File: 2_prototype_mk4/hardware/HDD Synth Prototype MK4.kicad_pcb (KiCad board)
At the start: 2 copper layers, 100.3 x 69.9 mm, 44 parts, among them J1 Micro_SD_Card, J3 Conn_02x20_Odd_Even, J4 1734451-1, J5 Conn_01x03_Pin, J6 171825-4, J7 Conn_01x04_Pin, J8 Conn_01x05, U1 MAX98357A, U2 Optocoupler_DC_PhotoNPN_AKEC, U3 TXS0101DBV

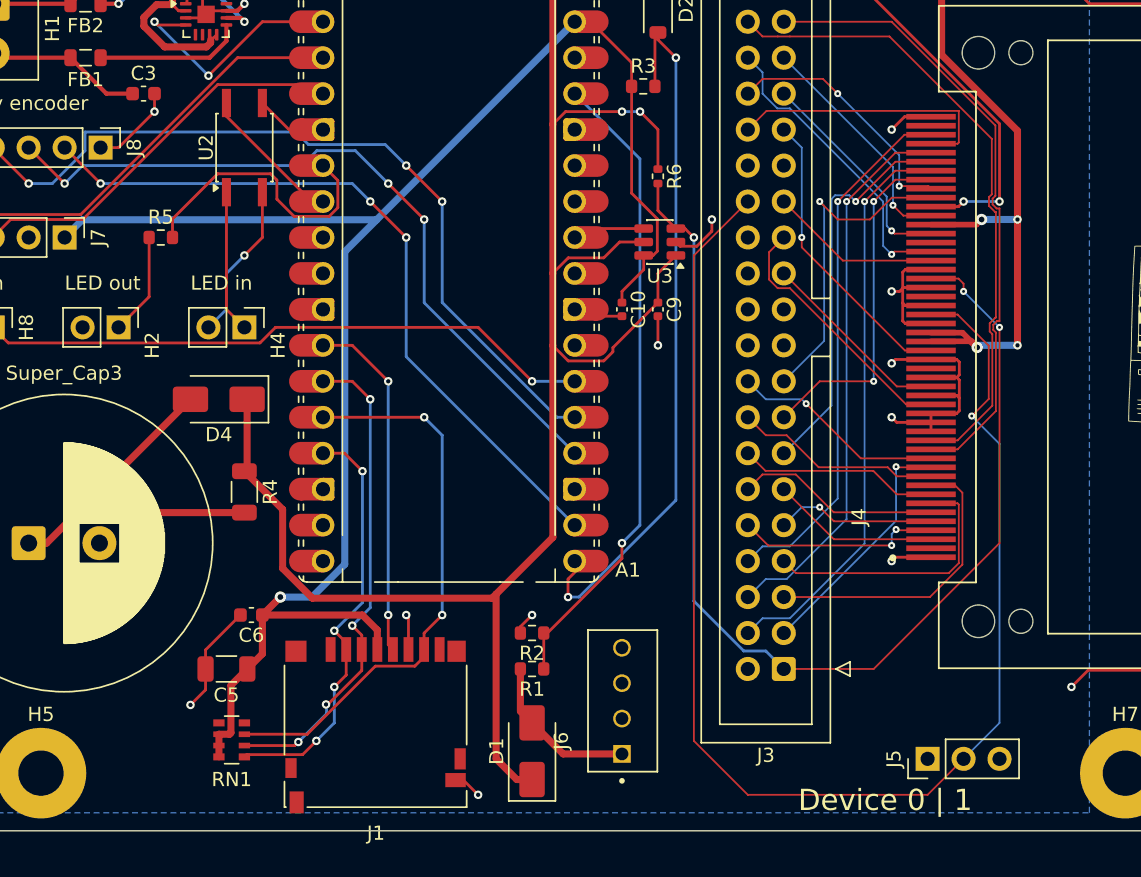
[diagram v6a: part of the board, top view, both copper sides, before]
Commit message: MKIV add RGB LED, reset jumper and fixed reset circuit
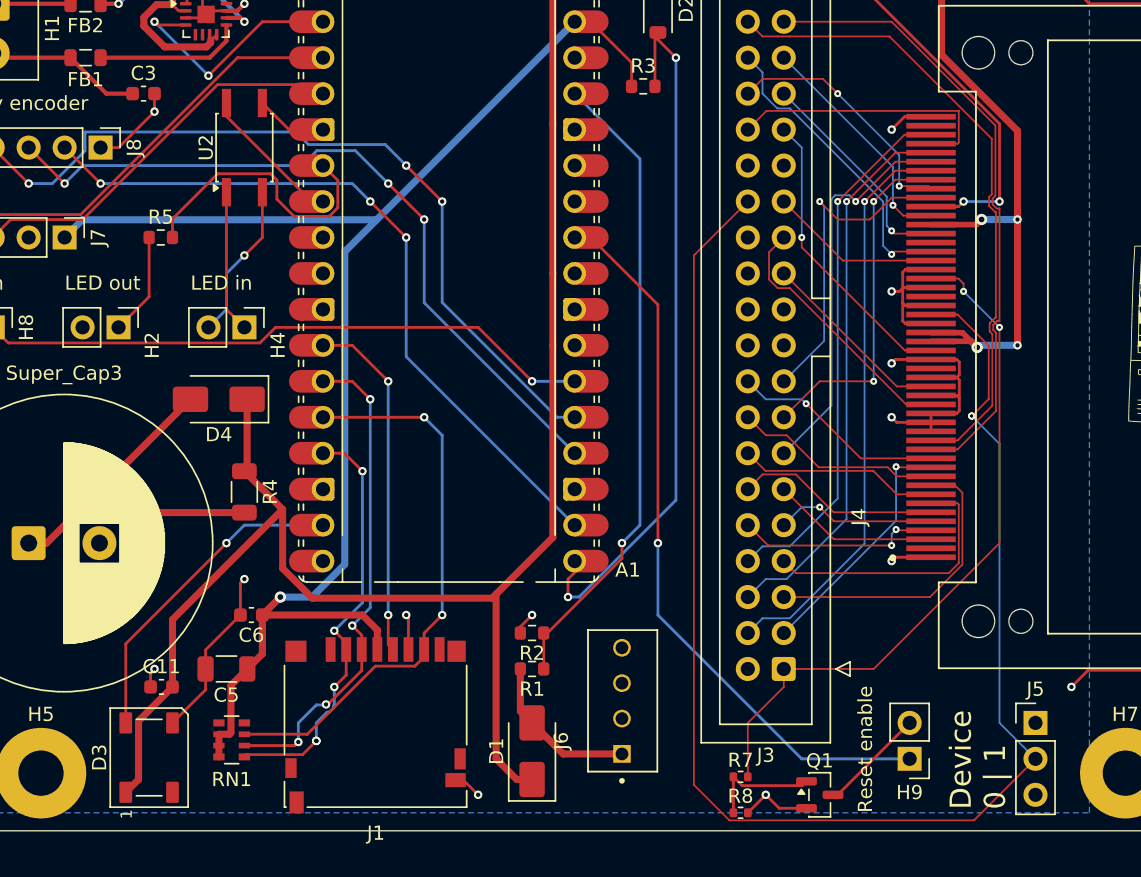
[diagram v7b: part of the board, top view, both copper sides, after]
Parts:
- removed C10, C9: 100nF, Capacitor_SMD:C_0402_1005Metric
- removed R6: 10K, Resistor_SMD:R_0402_1005Metric
- removed U3: TXS0101DBV, Package_TO_SOT_SMD:SOT-23-6
- added C11: 0.1uF, Capacitor_SMD:C_0603_1608Metric, F.Cu at (91.9, 106.7)
- added D3: WS2812B, LED_SMD:LED_WS2812B_PLCC4_5.0x5.0mm_P3.2mm, F.Cu at (91.1, 111.7)
- added H9: Conn_01x02, Connector_PinHeader_2.54mm:PinHeader_1x02_P2.54mm_Vertical, F.Cu at (144.8, 111.8)
- added Q1: MMBT3904, Package_TO_SOT_SMD:SOT-23, F.Cu at (138.4, 114.3)
- added R7: 4.7K, Resistor_SMD:R_0402_1005Metric, F.Cu at (132.8, 113.0)
- added R8: 10K, Resistor_SMD:R_0402_1005Metric, F.Cu at (132.8, 115.6)
- D2: value BAT43 -> BAT43W
- moved J5 8.03 mm to (153.7, 109.2), turned to 0 degrees
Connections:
- A1 pad 19: unconnected-(A1-GPIO14-Pad19)_1 -> /RGB LED/RGB_DATA
- D1 pad 2: POWER_5V_SUP -> +5V
- J6 pad 1: POWER_5V_SUP -> +5V
- R1 pad 2: POWER_5V_SUP -> +5V
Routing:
- net /Reset/PICO_RUN: track 5.14 -> 51.8 mm, vias 0 -> 1
- net /IDE_RESET: track 80.0 -> 49.4 mm, vias 3 -> 2
- net /RGB LED/RGB_DATA: track 0.00 -> 23.0 mm, vias 0 -> 1
- net POWER_5V_SUP: track 268.7 -> 249.8 mm, vias 6 -> 4
- net +3.3V: track 121.6 -> 104.2 mm
- net +5V: track 0.00 -> 11.4 mm
- net /IDE/CF_CABLE_SELECT: track 97.9 -> 106.3 mm, vias 1 -> 2
- net Net-(Q1-B): track 0.00 -> 8.08 mm
- net Net-(H9-Pin_2): track 0.00 -> 7.52 mm
- net GND: track 117.6 -> 118.9 mm
- net /SD card reader/SD_CS: track 30.8 -> 30.9 mm, vias 4 -> 5
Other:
- board text added: "Reset enable"

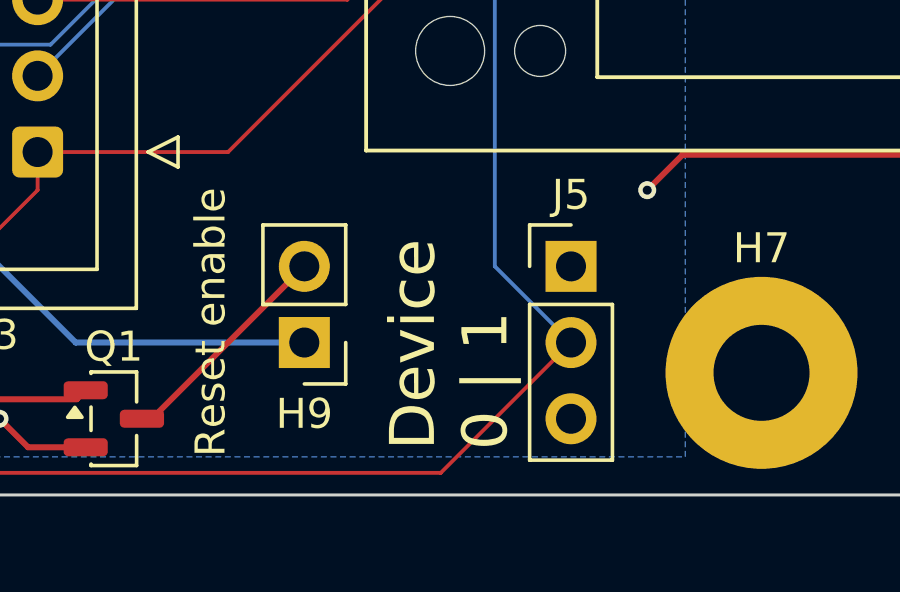
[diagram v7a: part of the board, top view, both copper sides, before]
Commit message: Make device select text consistent and correct
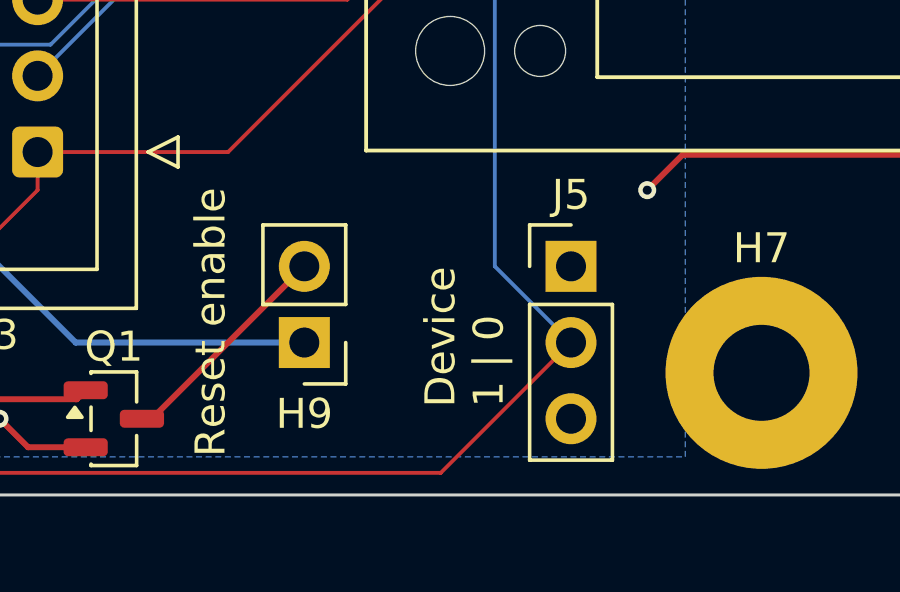
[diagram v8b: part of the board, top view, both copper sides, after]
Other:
- board text added: "Device 1 | 0"
- board text removed: "Device 0 | 1"
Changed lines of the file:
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@@
 		)
 	)
-	(gr_text "Device \n0 | 1"
-		(at 151.698425 115.341693 90)
+	(gr_text "Device \n1 | 0"
+		(at 151.513163 113.916837 90)
 		(layer "F.SilkS")
 		(effects
 			(font
-				(size 1.5 1.5)
+				(size 1 1)
 				(thickness 0.1875)
 			)
